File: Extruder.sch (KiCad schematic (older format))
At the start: 2 parts, among them J10 Probe, J11 Extruder Heater

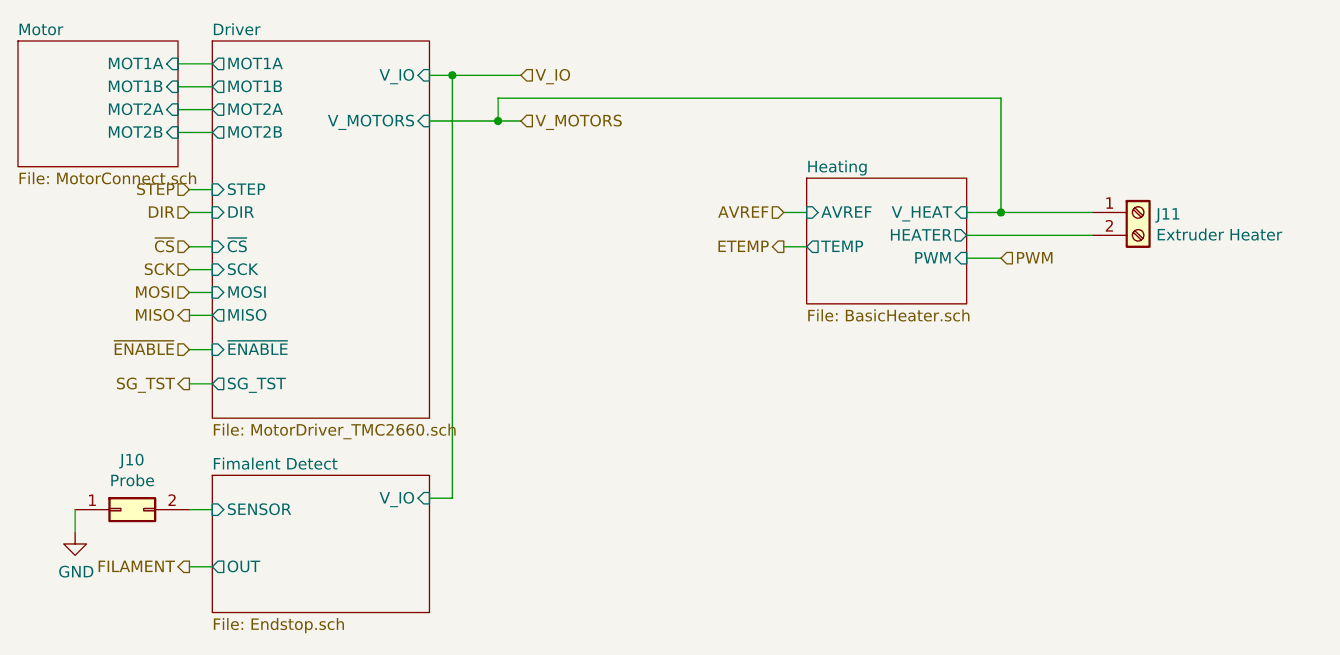
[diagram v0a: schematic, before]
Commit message: Added clock line for the motor drivers.
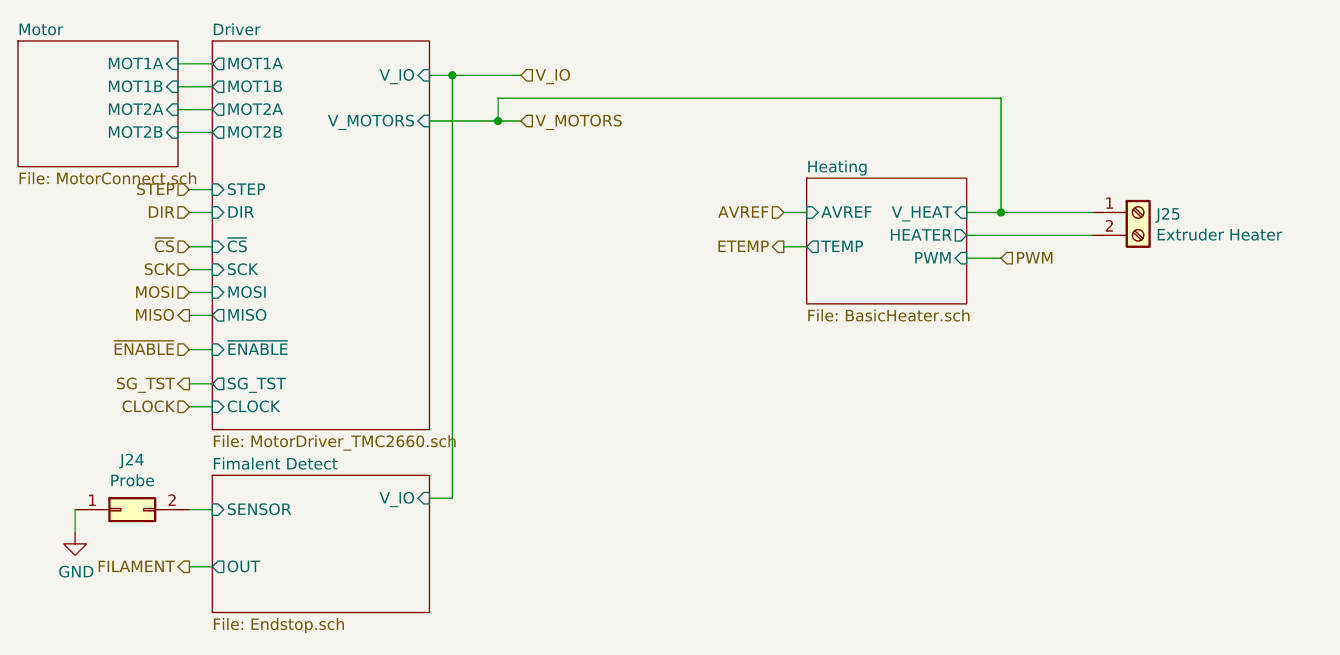
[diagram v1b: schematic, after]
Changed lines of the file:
@@
 $Descr A4 11693 8268
 encoding utf-8
-Sheet 3 34
+Sheet 25 34
 Title ""
 Date ""
@@
 $EndDescr
 $Sheet
-S 2700 1950 950  1650
+S 2700 1950 950  1700
 U 5AD4B0F5
 F0 "Driver" 50
@@
 F14 "~ENABLE" I L 2700 3300 50
 F15 "SG_TST" O L 2700 3450 50
+F16 "CLOCK" I L 2700 3550 50
 $EndSheet
 Text HLabel 2600 2600 0    50   Input ~ 0
@@
 AR Path="/5AC337B6/5ACBE919/5AD4BF35" Ref="J10"  Part="1"
 AR Path="/5AC337B6/5AD9F95A/5AD4BF35" Ref="J24"  Part="1"
-F 0 "J10" H 2350 4217 50  0000 C CNN
+F 0 "J24" H 2350 4217 50  0000 C CNN
 F 1 "Probe" H 2350 4126 50  0000 C CNN
 F 2 "Connector_PinHeader_2.54mm:PinHeader_1x02_P2.54mm_Vertical" H 2300 4000 50  0001 C CNN
@@
 AR Path="/5AC337B6/5ACBE919/5AD53BDD" Ref="J11"  Part="1"
 AR Path="/5AC337B6/5AD9F95A/5AD53BDD" Ref="J25"  Part="1"
-F 0 "J11" H 6829 2692 50  0000 L CNN
+F 0 "J25" H 6829 2692 50  0000 L CNN
 F 1 "Extruder Heater" H 6829 2601 50  0000 L CNN
 F 2 "TerminalBlock_Phoenix:TerminalBlock_Phoenix_PT-1,5-2-3.5-H_1x02_P3.50mm_Horizontal" H 6750 2700 50  0001 C CNN
@@
 	6550 2700 6150 2700
 Connection ~ 6150 2700
+Text HLabel 2600 3550 0    50   Input ~ 0
+CLOCK
+Wire Wire Line
+	2600 3550 2700 3550
 $EndSCHEMATC
